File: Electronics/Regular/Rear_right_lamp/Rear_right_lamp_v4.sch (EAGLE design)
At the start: 10 parts, among them X2 JST-XH-05-PIN-LONG-PAD

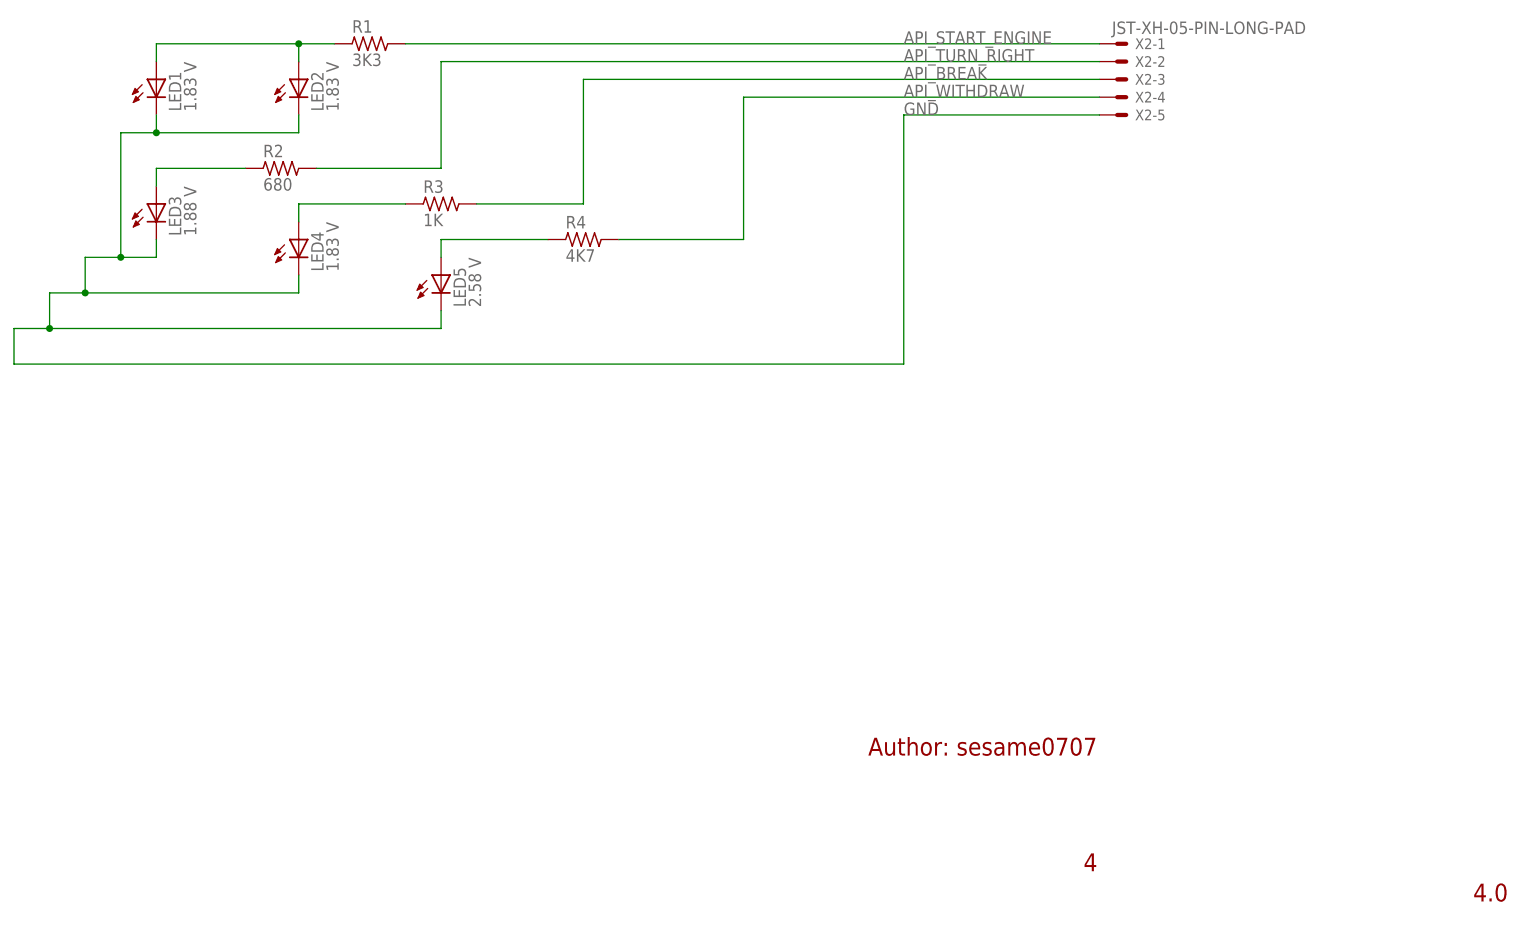
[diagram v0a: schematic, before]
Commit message: BOM on all the lamps added
Note: Version of lamps' projects has increased from x.0 to x.1.

What also has been done:
- some visual refactoring on schematics
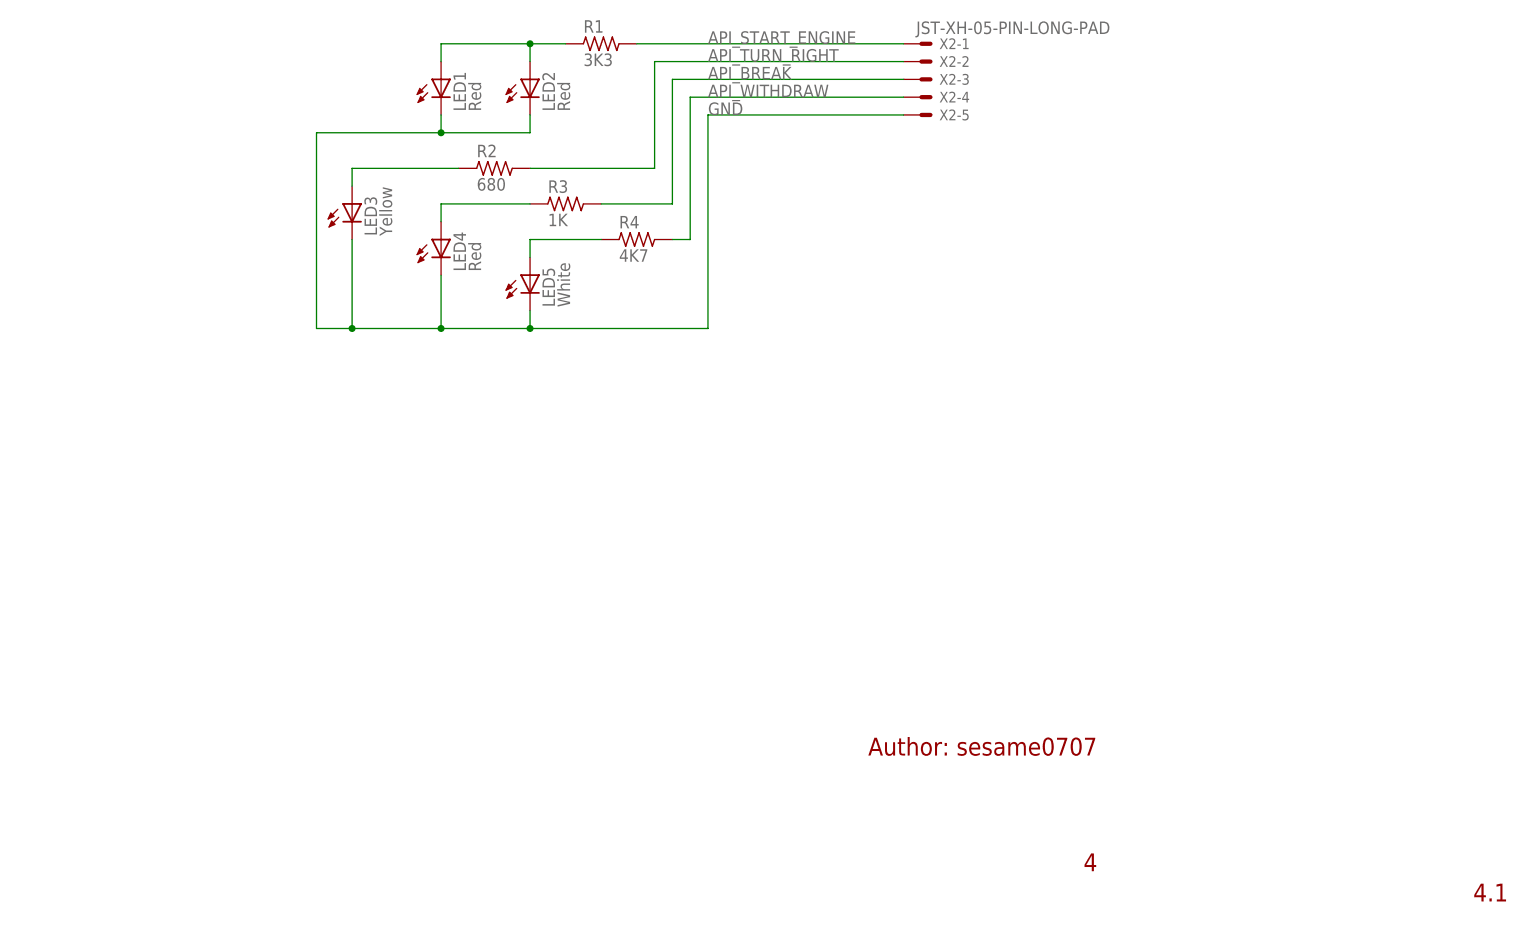
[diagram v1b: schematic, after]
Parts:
- LED1, LED2, LED4: value 1.83 V -> Red; CURRENT 1.48 mA -> (none); CURRENT_EMPIRICAL (none) -> 1.48 mA; MANUFACTURER (none) -> LUCKYLIGHT; MANUFACTURER_PART_NUMBER (none) -> LL-503VD2E-1B; SUPPLIER (none) -> TME; SUPPLIER_PART_NUMBER (none) -> LL-503VD2E-1B; SUPPLIER_URL (none) -> https://www.tme.eu/pl/details/ll-503vd2e-1b/diody-led-tht-o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; VOLTAGE_EMPIRICAL (none) -> 1.83 V
- LED3: value 1.88 V -> Yellow; CURRENT 1.42 mA -> (none); CURRENT_EMPIRICAL (none) -> 1.42 mA; MANUFACTURER (none) -> LUCKYLIGHT; MANUFACTURER_PART_NUMBER (none) -> LL-503YD2E-1B; SUPPLIER (none) -> TME; SUPPLIER_PART_NUMBER (none) -> LL-503YD2E-1B; SUPPLIER_URL (none) -> https://www.tme.eu/pl/details/ll-503yd2e-1b/diody-led-tht-o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; VOLTAGE_EMPIRICAL (none) -> 1.88 V
- LED5: value 2.58 V -> White; CURRENT 0.14 mA -> (none); CURRENT_EMPIRICAL (none) -> 0.14 mA; MANUFACTURER (none) -> LUCKYLIGHT; MANUFACTURER_PART_NUMBER (none) -> LL-504WC2V-W2-3PD; SUPPLIER (none) -> TME; SUPPLIER_PART_NUMBER (none) -> LL-504WC2V-W2-3PD; SUPPLIER_URL (none) -> https://www.tme.eu/pl/details/ll-504wc2v-w2-3pd/diody-led-t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; VOLTAGE_EMPIRICAL (none) -> 2.58 V
- R1: MANUFACTURER (none) -> ROYAL OHM; MANUFACTURER_PART_NUMBER (none) -> 1206S4J0332T5E; RESISTANCE (none) -> 3.3 kOhm; SUPPLIER (none) -> TME; SUPPLIER_PART_NUMBER (none) -> 1206S4J0332T5E; SUPPLIER_URL (none) -> https://www.tme.eu/pl/details/1206s4j0332t5e/rezystory-smd/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
- R2: MANUFACTURER (none) -> ROYAL OHM; MANUFACTURER_PART_NUMBER (none) -> 1206S4J0681T5E; RESISTANCE (none) -> 680 Ohm; SUPPLIER (none) -> TME; SUPPLIER_PART_NUMBER (none) -> 1206S4J0681T5E; SUPPLIER_URL (none) -> https://www.tme.eu/pl/details/1206s4j0681t5e/rezystory-smd/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
- R3: MANUFACTURER (none) -> ROYAL OHM; MANUFACTURER_PART_NUMBER (none) -> 1206S4J0102T5E; RESISTANCE (none) -> 1 kOhm; SUPPLIER (none) -> TME; SUPPLIER_PART_NUMBER (none) -> 1206S4J0102T5E; SUPPLIER_URL (none) -> https://www.tme.eu/pl/details/1206s4j0102t5e/rezystory-smd/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
- R4: MANUFACTURER (none) -> ROYAL OHM; MANUFACTURER_PART_NUMBER (none) -> 1206S4J0472T5E; RESISTANCE (none) -> 4.7 kOhm; SUPPLIER (none) -> TME; SUPPLIER_PART_NUMBER (none) -> 1206S4J0472T5E; SUPPLIER_URL (none) -> https://www.tme.eu/pl/details/1206s4j0472t5e/rezystory-smd/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
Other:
- note added: "4.1"
- note removed: "4.0"
- moved on the sheet: LED1, LED2, LED3, LED4, LED5, R1, R2, R3, R4, X2-1, X2-2, X2-3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
